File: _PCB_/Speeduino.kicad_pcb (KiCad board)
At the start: 2 copper layers, 100 x 100 mm, 43 parts, among them U1 TC4424AVOA, U2 TC4424AVOA

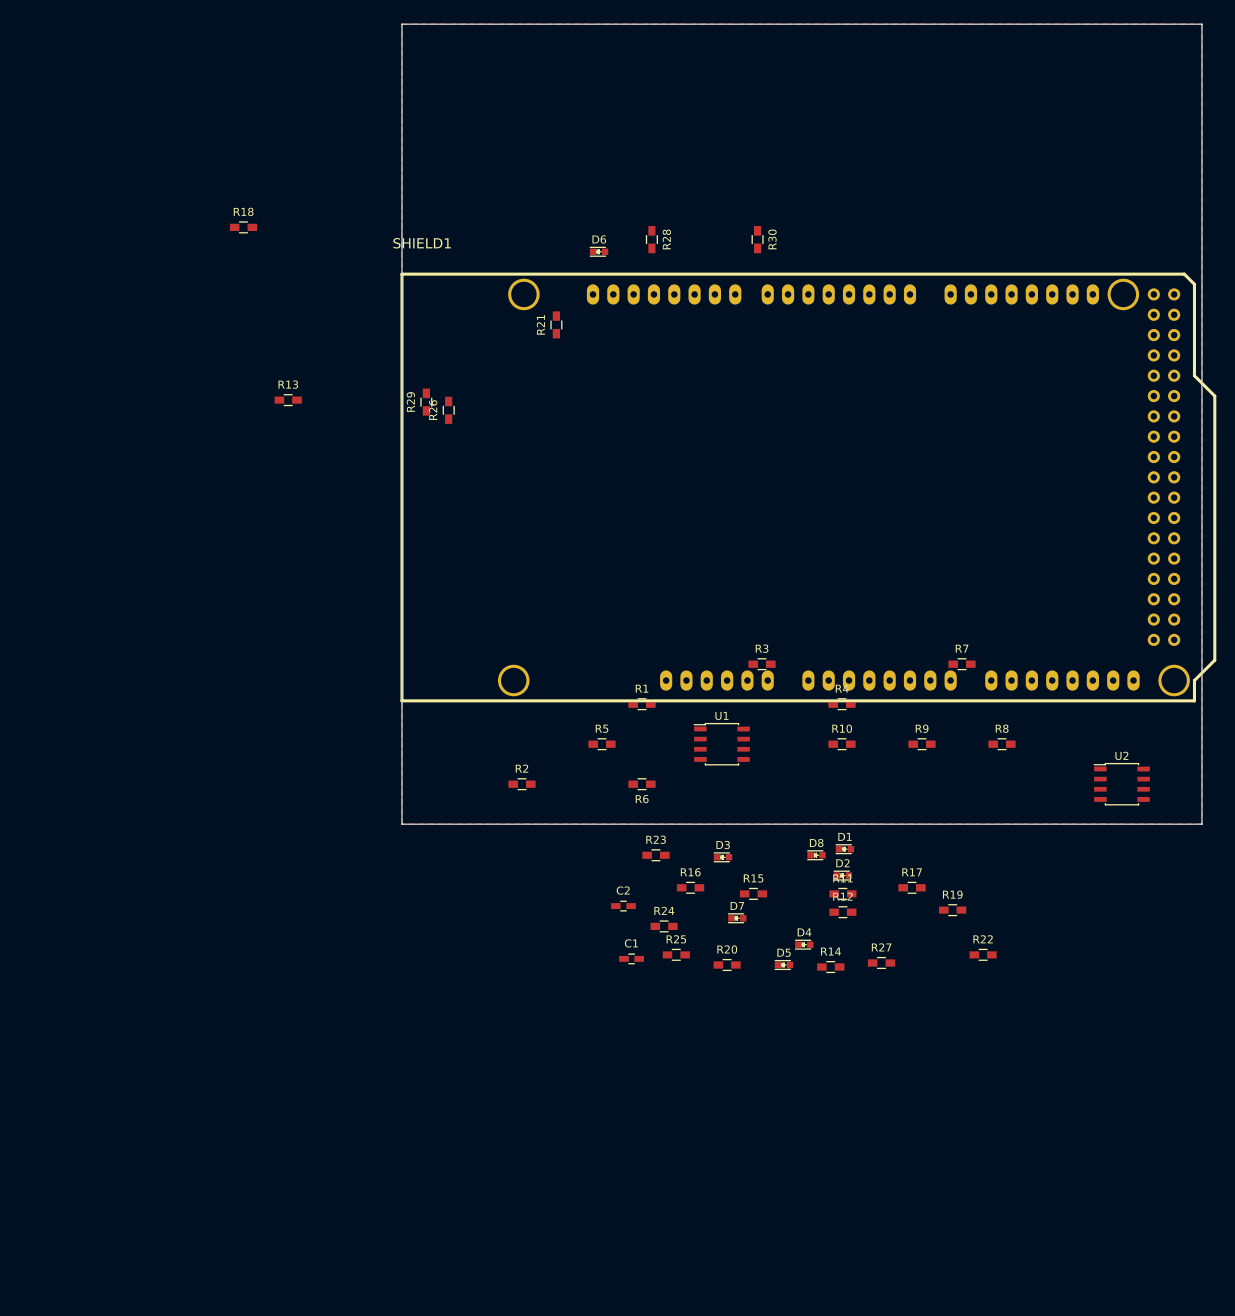
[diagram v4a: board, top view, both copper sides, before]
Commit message: modification sortie injecteur
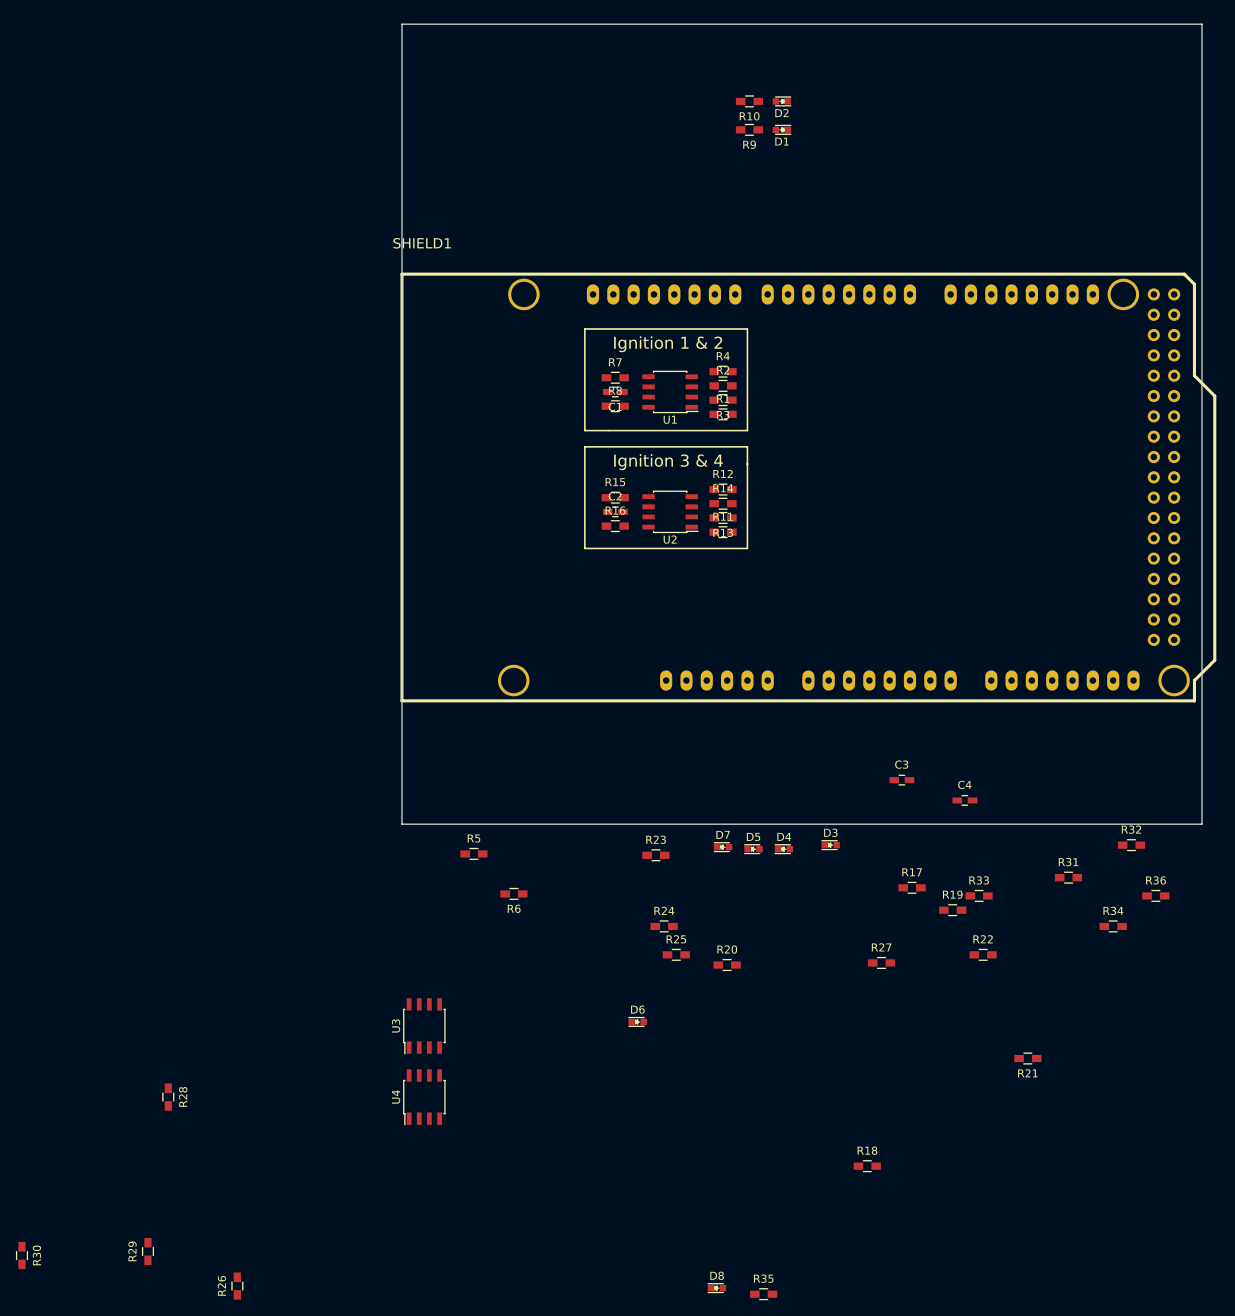
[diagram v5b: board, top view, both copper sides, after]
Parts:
- added C3: C, Speeduino:C_0603_HandSoldering, F.Cu at (142.5, 124.5)
- added C4: C, Speeduino:C_0603_HandSoldering, F.Cu at (150.4, 127.0)
- added R31: 100K, Speeduino:R_0603_HandSoldering, F.Cu at (163.3, 136.7)
- added R32: 100K, Speeduino:R_0603_HandSoldering, F.Cu at (171.2, 132.6)
- added R33: R, Speeduino:R_0603_HandSoldering, F.Cu at (152.1, 139.0)
- added R34: R, Speeduino:R_0603_HandSoldering, F.Cu at (168.9, 142.8)
- added R35: R, Speeduino:R_0603_HandSoldering, F.Cu at (125.2, 188.8)
- added R36: R, Speeduino:R_0603_HandSoldering, F.Cu at (174.2, 139.0)
- added U3: TC4424AVOA, Speeduino:SOIC-8_3.9x4.9mm_Pitch1.27mm, F.Cu at (82.8, 155.2)
- added U4: TC4424AVOA, Speeduino:SOIC-8_3.9x4.9mm_Pitch1.27mm, F.Cu at (82.8, 164.1)
- R10, R25, R26, R27, R9: value 100K -> R
- R11, R12: value R -> 1K
- R13, R14: value R -> 100K
- R19: value 680 -> 1K
- R20: value 100K -> 1K
- R21: value 1K -> 100K
- R22: value 680 -> 100K
- R23, R24: value 680 -> 0
- R28, R7, R8: value 1K -> R
- moved R30 156.8 mm to (32.5, 183.9)
- moved R18 140.9 mm to (138.2, 172.7)
- moved R28 123.1 mm to (50.8, 164.1)
- moved R26 112.6 mm to (59.4, 187.7)
- moved R29 111.7 mm to (48.2, 183.4)
- moved R21 109.0 mm to (158.2, 159.3), turned to 180 degrees
- moved D2 97.1 mm to (127.5, 39.7), turned to 180 degrees
- moved D6 96.4 mm to (109.5, 154.7)
- moved D1 90.3 mm to (127.5, 43.2), turned to 180 degrees
- moved R10 81.2 mm to (123.4, 39.7), turned to 180 degrees
- moved R9 79.8 mm to (123.4, 43.2), turned to 180 degrees
- moved C1 70.9 mm to (106.7, 76.0), turned to 180 degrees
- moved U2 65.9 mm to (113.5, 91.0), turned to 180 degrees
- moved R8 64.2 mm to (106.7, 77.8)
- moved R14 59.5 mm to (120.1, 89.9)
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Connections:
- D5 pad 1: Net-(D5-Pad1) -> GND
- D5 pad 2: INJ3-CPU-D10 -> Net-(D5-Pad2)
- D6 pad 1: Net-(D6-Pad1) -> GND
- D6 pad 2: INJ4-CPU-D11 -> Net-(D6-Pad2)
- D7 pad 1: Net-(D7-Pad1) -> GND
- D7 pad 2: INJ1-CPU-D8 -> Net-(D7-Pad2)
- D8 pad 1: Net-(D8-Pad1) -> GND
- D8 pad 2: INJ2-CPU-D9 -> Net-(D8-Pad2)
- R1 pad 2: (no net) -> IGN1_CPU_D40
- R10 pad 1: Net-(R10-Pad1) -> Net-(D2-Pad2)
- R10 pad 2: GND -> ING-1-OUT
- R11 pad 1: ING-2-OUT -> Net-(R11-Pad1)
- R11 pad 2: Net-(R11-Pad2) -> IGN3_CPU_D52
- R12 pad 1: ING-1-OUT -> Net-(R12-Pad1)
- R12 pad 2: Net-(R12-Pad2) -> IGN4_CPU_D50
- R13 pad 1: Net-(D1-Pad2) -> GND
- R13 pad 2: ING-2-OUT -> Net-(R11-Pad1)
- R14 pad 1: Net-(D2-Pad2) -> Net-(R12-Pad1)
- R14 pad 2: ING-1-OUT -> GND
- R19 pad 1: GND -> Net-(R19-Pad1)
- R19 pad 2: Net-(D5-Pad1) -> (no net)
- R2 pad 2: (no net) -> IGN2_CPU_D38
- R20 pad 1: INJ3-CPU-D10 -> Net-(R20-Pad1)
- R20 pad 2: GND -> (no net)
- R21 pad 1: (no net) -> GND
- R21 pad 2: INJ3-CPU-D10 -> Net-(R19-Pad1)
- R22 pad 1: GND -> Net-(R20-Pad1)
- R22 pad 2: Net-(D6-Pad1) -> GND
- R23 pad 1: GND -> VCC_INJECTOR
- R23 pad 2: Net-(D7-Pad1) -> +5V
- R24 pad 1: GND -> +12V
- R24 pad 2: Net-(D8-Pad1) -> VCC_INJECTOR
- R25 pad 1: INJ4-CPU-D11 -> INJ-2-OUT
- R25 pad 2: GND -> Net-(R25-Pad2)
- R26 pad 1: INJ1-CPU-D8 -> INJ-1-OUT
- R26 pad 2: GND -> Net-(R26-Pad2)
- R27 pad 1: INJ2-CPU-D9 -> Net-(D5-Pad2)
- R27 pad 2: GND -> INJ-2-OUT
- R28 pad 1: (no net) -> Net-(D6-Pad2)
- R28 pad 2: INJ4-CPU-D11 -> INJ-1-OUT
- R29 pad 1: (no net) -> Net-(R29-Pad1)
- R29 pad 2: INJ1-CPU-D8 -> (no net)
- R30 pad 1: (no net) -> Net-(R30-Pad1)
- R30 pad 2: INJ2-CPU-D9 -> (no net)
- R5 pad 2: (no net) -> +5V
- R6 pad 1: (no net) -> +12V
- R7 pad 1: Net-(R7-Pad1) -> ING-2-OUT
- R7 pad 2: (no net) -> Net-(R7-Pad2)
- R8 pad 1: Net-(R10-Pad1) -> ING-1-OUT
- R8 pad 2: (no net) -> Net-(R8-Pad2)
- R9 pad 1: GND -> Net-(D1-Pad2)
- R9 pad 2: Net-(R7-Pad1) -> ING-2-OUT
- SHIELD1 pad 38: (no net) -> IGN2_CPU_D38
- SHIELD1 pad 40: (no net) -> IGN1_CPU_D40
- SHIELD1 pad 50: (no net) -> IGN4_CPU_D50
- SHIELD1 pad 52: (no net) -> IGN3_CPU_D52
- SHIELD1 pad GND3: (no net) -> GND
- SHIELD1 pad GND4: (no net) -> GND
- SHIELD1 pad GND5: (no net) -> GND
- U1 pad 5: Net-(R11-Pad2) -> Net-(R7-Pad2)
- U1 pad 7: Net-(R12-Pad2) -> Net-(R8-Pad2)
- U2 pad 2: Net-(R7-Pad1) -> Net-(R11-Pad1)
- U2 pad 4: Net-(R10-Pad1) -> Net-(R12-Pad1)
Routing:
- removed copper zone on F.Cu, net GND
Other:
- board text added: "Ignition 1 & 2"
- board text added: "Ignition 3 & 4"

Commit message: routage des sorties de semi puissance !!
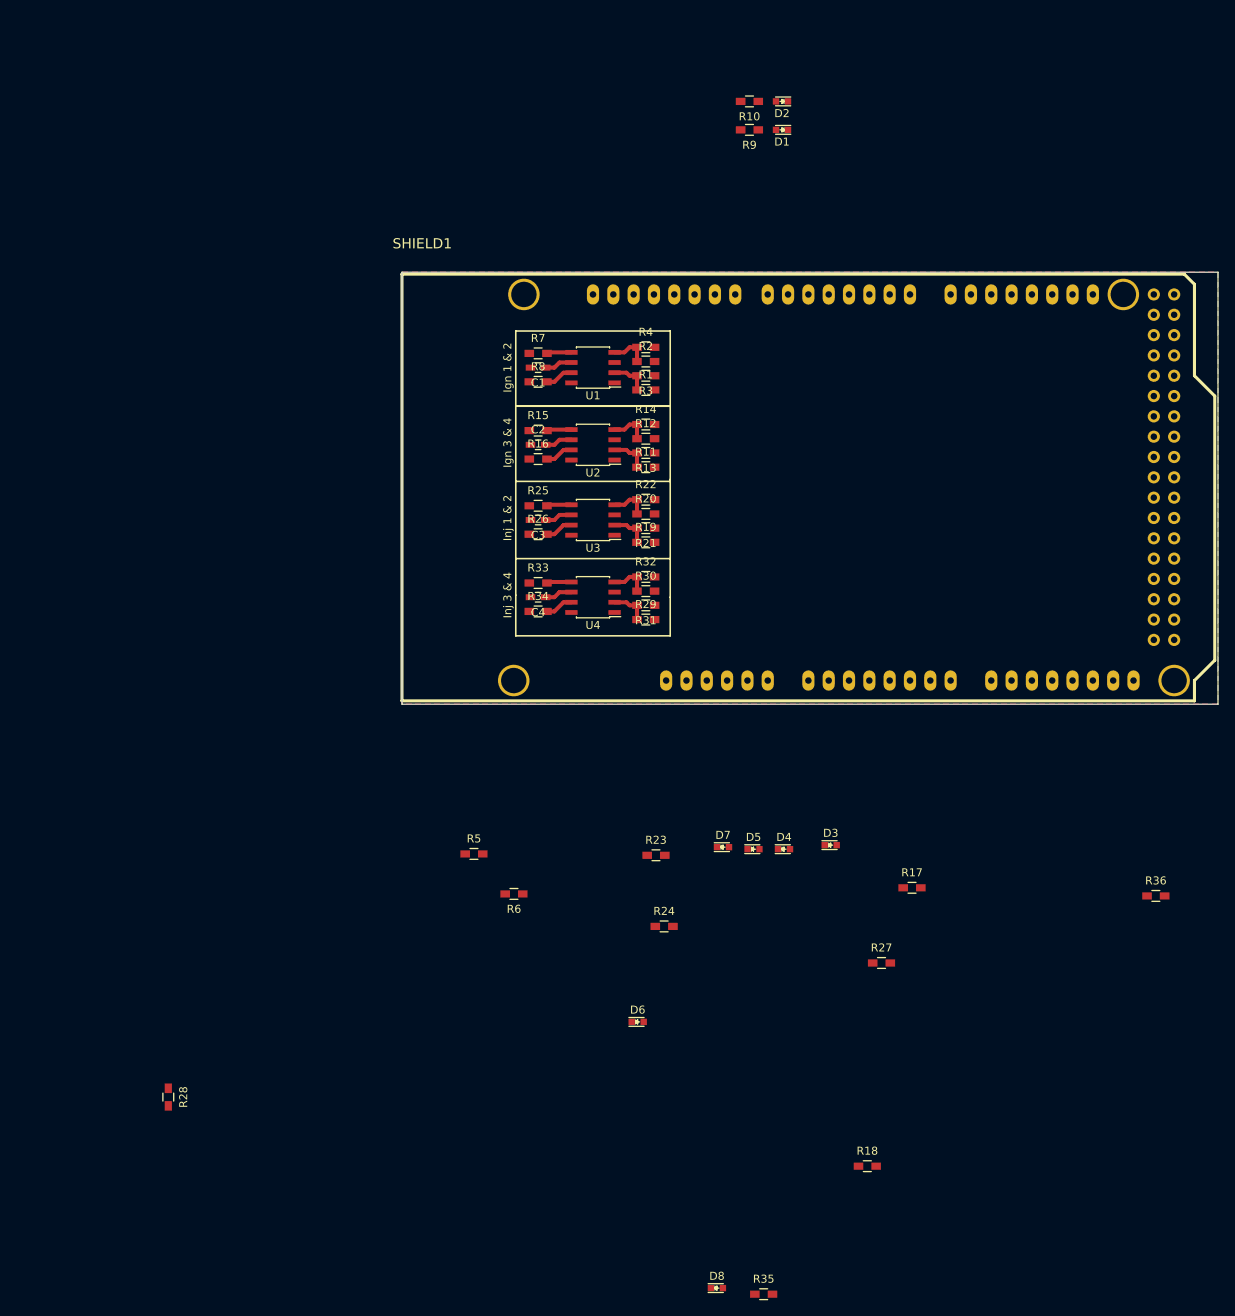
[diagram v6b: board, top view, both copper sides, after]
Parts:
- moved R30 113.9 mm to (110.5, 100.9), turned to 0 degrees
- moved R26 101.2 mm to (97.0, 93.8), turned to 0 degrees
- moved R29 100.6 mm to (110.5, 104.4), turned to 0 degrees
- moved R34 82.0 mm to (97.0, 103.4)
- moved R21 81.7 mm to (110.5, 93.0)
- moved R22 70.8 mm to (110.5, 89.4)
- moved R32 69.3 mm to (110.5, 99.1)
- moved R33 67.6 mm to (97.0, 99.8)
- moved U3 66.7 mm to (103.9, 92.0), turned to 180 degrees
- moved U4 65.9 mm to (103.9, 101.6), turned to 180 degrees
- moved R31 62.8 mm to (110.5, 102.6), turned to 180 degrees
- moved R19 59.9 mm to (110.5, 94.8)
- moved C4 59.1 mm to (97.0, 101.6), turned to 180 degrees
- moved R25 58.7 mm to (97.0, 90.2)
- moved R20 57.3 mm to (110.5, 91.2)
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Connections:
- R19 pad 2: (no net) -> INJ1_CPU_D8
- R20 pad 2: (no net) -> INJ2_CPU_D9
- R29 pad 2: (no net) -> INJ3_CPU_D10
- R30 pad 2: (no net) -> INJ4_CPU_D11
- SHIELD1 pad 10: (no net) -> INJ3_CPU_D10
- SHIELD1 pad 11: (no net) -> INJ4_CPU_D11
- SHIELD1 pad 8: (no net) -> INJ1_CPU_D8
- SHIELD1 pad 9: (no net) -> INJ2_CPU_D9
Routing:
- net VCC_INJECTOR: track 0.00 -> 6.94 mm
- net VCC_IGNITION: track 0.00 -> 6.94 mm
- net Net-(R30-Pad1): track 0.00 -> 4.85 mm
- net Net-(R2-Pad1): track 0.00 -> 4.85 mm
- net Net-(R12-Pad1): track 0.00 -> 4.85 mm
- net Net-(R20-Pad1): track 0.00 -> 4.85 mm
- net Net-(R11-Pad1): track 0.00 -> 4.74 mm
- net Net-(R1-Pad1): track 0.00 -> 4.74 mm
- net Net-(R29-Pad1): track 0.00 -> 4.74 mm
- net Net-(R19-Pad1): track 0.00 -> 4.74 mm
- net Net-(R34-Pad2): track 0.00 -> 3.53 mm
- net Net-(R26-Pad2): track 0.00 -> 3.53 mm
- net Net-(R16-Pad2): track 0.00 -> 3.53 mm
- net Net-(R8-Pad2): track 0.00 -> 3.53 mm
- net Net-(R7-Pad2): track 0.00 -> 3.11 mm
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- added copper zone on F.Cu, net GND
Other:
- board size 100 x 100 mm -> 102 x 54 mm
- board text added: "Ign 1 & 2"
- board text added: "Ign 3 & 4"
- board text added: "Inj 1 & 2"
- board text added: "Inj 3 & 4"
- board text removed: "Ignition 1 & 2"
- board text removed: "Ignition 3 & 4"
